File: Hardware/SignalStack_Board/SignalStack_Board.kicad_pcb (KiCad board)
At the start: 2 copper layers, 101.6 x 67.6 mm, 64 parts, among them J1 Molex_uF_SV_06, J2 RJ45_LED_Shielded, J3 Molex_uF_SV_06, Q1 SI4156DY, Q2 SI4156DY, Q3 SI4156DY, Q4 SI4156DY, Q5 SI4156DY, Q6 SI4156DY, Q7 SI4156DY, Q8 SI4156DY, U1 OKI, U2 SMAJ12CA, U3 Teensy4.1_DEV-16771, U4 TSR_1-2450, U5 IRS2005S, U6 IRS2005S, U8 IRS2005S, U9 IRS2005S

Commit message: Worked on layout a lot
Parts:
- J1: footprint MRDT_Connectors:MOLEX_uF_S_06_Vertical -> Connector_PinHeader_2.00mm:PinHeader_2x03_P2.00mm_Vertical
- moved U2 173.6 mm to (189.2, 110.0)
- moved C3 136.9 mm to (188.6, 112.8)
- moved C2 125.7 mm to (168.8, 103.6), turned to 180 degrees
- moved U5 124.7 mm to (213.9, 105.8)
- moved C4 119.5 mm to (188.6, 114.8)
- moved J1 116.2 mm to (174.8, 113.3)
- moved C6 94.9 mm to (175.8, 125.2), turned to 180 degrees
- moved U1 81.4 mm to (176.3, 101.0), turned to 180 degrees
- moved C5 80.4 mm to (188.6, 116.8)
- moved C1 78.0 mm to (173.5, 103.6), turned to 180 degrees
- moved J2 67.9 mm to (149.7, 119.2), turned to -90 degrees
- moved U4 61.1 mm to (161.0, 98.3), turned to 180 degrees
- moved Conn1 12.2 mm to (192.5, 102.9)
- moved U3 3.81 mm to (142.7, 103.9)
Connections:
- net Net-(J1-Pad1) renamed /TX+
- net Net-(J1-Pad2) renamed /TX-
- net Net-(J1-Pad5) renamed /RX-
- net Net-(J1-Pad6) renamed /RX+
- Conn1 pad 2: (no net) -> +12V
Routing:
- net +5V: track 0.00 -> 152.9 mm, vias 0 -> 2
- net GPS RX: track 0.00 -> 86.8 mm
- net GPS TX: track 0.00 -> 86.7 mm
- net +3V3: track 0.00 -> 61.9 mm, vias 0 -> 4
- net +12V: track 0.00 -> 38.2 mm
- net Net-(J1-Pad4): track 0.00 -> 28.2 mm
- net Net-(C6-Pad1): track 0.00 -> 21.8 mm, vias 0 -> 1
- net /TX-: track 0.00 -> 15.1 mm
- net /TX+: track 0.00 -> 14.3 mm
- net Net-(C6-Pad2): track 0.00 -> 13.5 mm
- net /RX+: track 0.00 -> 8.16 mm
- net /RX-: track 0.00 -> 8.05 mm
- net GND: vias 0 -> 3
- added copper zone on F.Cu, net +12V

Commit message: Worked on layout
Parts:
- Conn1: moved to B.Cu
- moved D1 138.1 mm to (163.8, 107.4)
- moved D3 118.9 mm to (157.7, 107.4)
- moved U9 118.0 mm to (207.0, 114.9)
- moved D2 99.6 mm to (177.7, 107.7)
- moved U6 98.0 mm to (207.0, 123.1)
- moved U8 83.3 mm to (207.0, 97.0)
- moved R3 79.5 mm to (157.6, 105.2)
- moved R2 77.5 mm to (181.6, 107.7)
- moved R1 67.0 mm to (167.5, 107.4), turned to 180 degrees
- moved U2 61.2 mm to (128.0, 112.0)
- moved C3 60.6 mm to (128.0, 114.8)
- moved C4 60.6 mm to (128.0, 116.8)
- moved C5 60.6 mm to (128.0, 118.9)
- moved Conn1 8.00 mm to (184.5, 102.9)
- moved U5 7.04 mm to (206.9, 104.9)
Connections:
- U3 pad 18: IMU Data -> I2C SDA
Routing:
- net I2C SDA: track 0.00 -> 77.4 mm, vias 0 -> 2
- net I2C SCL: track 0.00 -> 74.4 mm, vias 0 -> 1
- net Coil1+: track 0.00 -> 49.7 mm, vias 0 -> 2
- net Coil1-: track 0.00 -> 47.8 mm, vias 0 -> 3
- net Coil2-: track 0.00 -> 45.1 mm, vias 0 -> 2
- net Coil2+: track 0.00 -> 44.3 mm, vias 0 -> 3
- net +5V: track 152.9 -> 128.0 mm, vias 2 -> 4
- net +12V: track 38.2 -> 21.8 mm
- net Net-(D3-Pad2): track 0.00 -> 2.31 mm
- net +3V3: track 61.9 -> 64.2 mm
- net Net-(D2-Pad2): track 0.00 -> 2.14 mm
- net Net-(D1-Pad2): track 0.00 -> 1.92 mm
- net GND: track 0.00 -> 0.20 mm, vias 3 -> 4

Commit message: Finished layout
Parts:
- added G***: LOGO, MRDT_Silkscreens:0_MRDT_Logo_20mm, B.Cu at (183.4, 118.5)
- moved R16 195.2 mm to (228.2, 131.2), turned to 180 degrees
- moved D4 183.8 mm to (205.0, 100.8), turned to 180 degrees
- moved D8 183.5 mm to (204.3, 92.1), turned to 90 degrees
- moved D5 179.5 mm to (205.0, 118.7), turned to 180 degrees
- moved R5 179.3 mm to (209.0, 118.7), turned to 180 degrees
- moved D11 175.0 mm to (205.0, 111.0), turned to 180 degrees
- moved R7 171.3 mm to (209.0, 126.9), turned to 180 degrees
- moved D6 170.5 mm to (205.0, 108.7), turned to 180 degrees
- moved R15 168.3 mm to (223.5, 89.0)
- moved D9 167.4 mm to (218.1, 127.1)
- moved R9 167.0 mm to (214.5, 108.7)
- moved D10 164.1 mm to (206.8, 92.1), turned to 90 degrees
- moved C11 161.3 mm to (230.4, 119.4), turned to 90 degrees
- moved D7 158.7 mm to (205.0, 126.9), turned to 180 degrees
- moved C8 154.7 mm to (218.1, 128.9)
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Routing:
- net +12V: track 21.8 -> 163.7 mm
- net /M+: track 0.00 -> 114.2 mm, vias 0 -> 5
- net /M-: track 0.00 -> 93.5 mm, vias 0 -> 5
- net Net-(R17-Pad1): track 0.00 -> 51.9 mm, vias 0 -> 2
- net Net-(Q7-Pad4): track 0.00 -> 42.4 mm, vias 0 -> 2
- net Net-(Q8-Pad4): track 0.00 -> 36.8 mm, vias 0 -> 2
- net Net-(R16-Pad1): track 0.00 -> 34.8 mm, vias 0 -> 2
- net Net-(R10-Pad1): track 0.00 -> 22.9 mm, vias 0 -> 2
- net Net-(C7-Pad1): track 0.00 -> 21.4 mm, vias 0 -> 2
- net Net-(R15-Pad1): track 0.00 -> 20.4 mm, vias 0 -> 2
- net Net-(R12-Pad1): track 0.00 -> 18.1 mm, vias 0 -> 2
- net Net-(R9-Pad1): track 0.00 -> 16.6 mm, vias 0 -> 2
- net Net-(C8-Pad1): track 0.00 -> 14.3 mm, vias 0 -> 2
- net Net-(Q5-Pad4): track 0.00 -> 11.8 mm
- net Net-(R11-Pad1): track 0.00 -> 11.4 mm, vias 0 -> 2
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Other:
- outline, holes or cut-outs redrawn
- board text added: "Coil 1"
- board text added: "Coil 2"
- board text added: "GPS"
- board text added: "Signal Stack Board, 2023 Rev 1 Mars Rover Design Team Grant Brinker"
- board text added: "Super Spicy Signal Stack Spinning System"

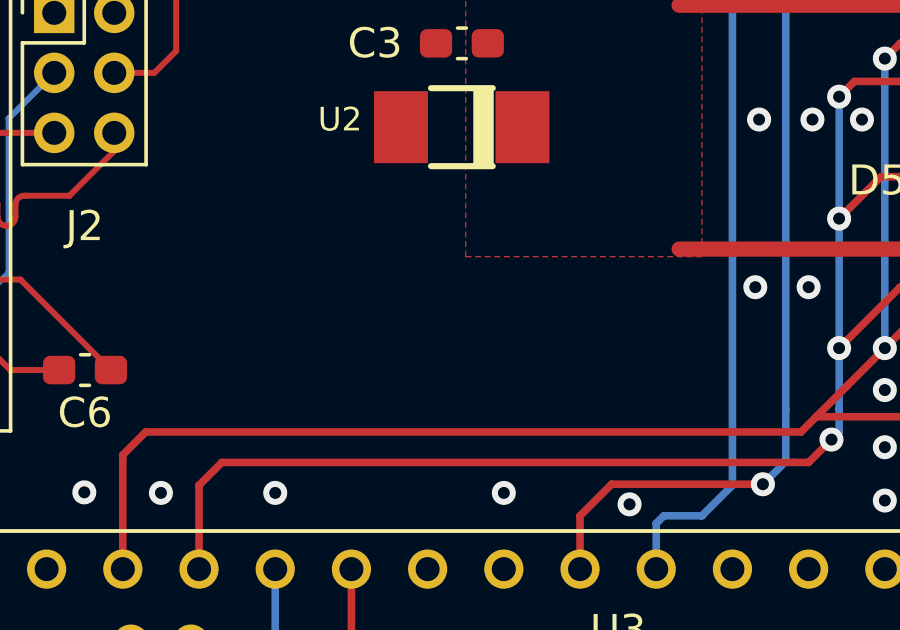
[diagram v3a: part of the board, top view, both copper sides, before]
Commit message: Added silkscreen
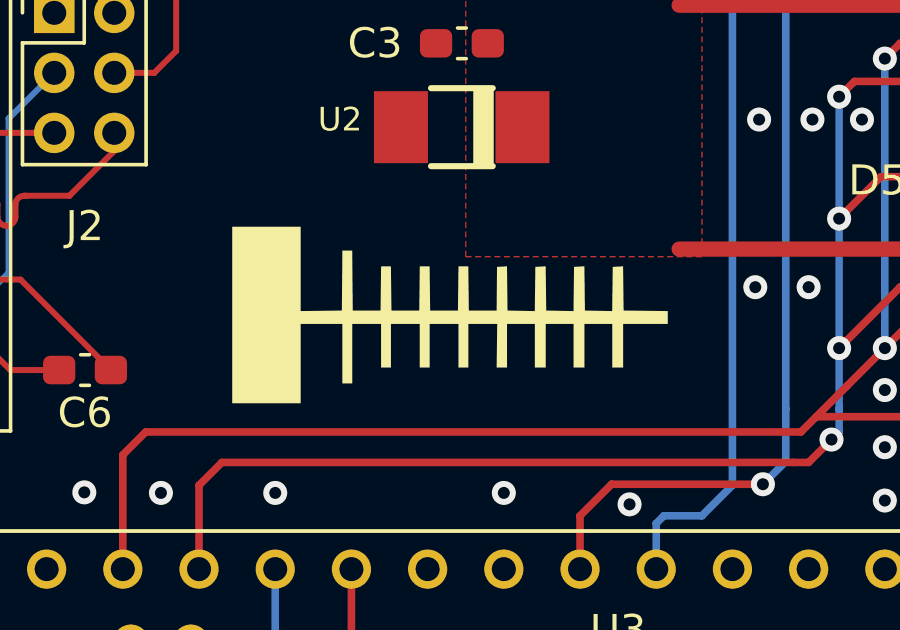
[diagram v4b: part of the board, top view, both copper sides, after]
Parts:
- added G***: LOGO, MRDT_Silkscreens:yagi, F.Cu at (188.0, 123.2)
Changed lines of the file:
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@@
     )
+  )
+  (footprint "MRDT_Silkscreens:yagi" (layer "F.Cu")
+    (at 187.96 123.19)
+    (attr board_only exclude_from_pos_files exclude_from_bom)
+    (fp_text reference "G***" (at 0 0) (layer "F.SilkS") hide
+      (effects (font (size 1.524 1.524) (thickness 0.3)))
+    )
+    (fp_text value "LOGO" (at 0.75 0) (layer "F.SilkS") hide
+      (effects (font (size 1.524 1.524) (thickness 0.3)))
+    )
+    (fp_poly (pts
+        (xy -4.994011 0.034415)
+        (xy -4.307748 0.025475)
+        (xy -3.621485 0.016536)
+        (xy -3.612732 -0.98392)
+        (xy -3.603978 -1.984375)
+        (xy -3.275189 -1.984375)
+        (xy -3.266436 -0.98392)
+        (xy -3.257683 0.016536)
+        (xy -2.331641 0.016536)
+        (xy -2.32274 -0.719336)
+        (xy -2.313839 -1.455209)
+        (xy -1.985641 -1.455209)
+        (xy -1.97674 -0.719336)
+        (xy -1.967839 0.016536)
+        (xy -1.041797 0.016536)
+        (xy -1.032896 -0.719336)
+        (xy -1.023995 -1.455209)
+        (xy -0.695797 -1.455209)
+        (xy -0.686896 -0.719336)
+        (xy -0.677995 0.016536)
+        (xy 0.248046 0.016536)
+        (xy 0.256947 -0.719336)
+        (xy 0.265848 -1.455209)
+        (xy 0.594047 -1.455209)
+        (xy 0.602948 -0.719336)
+        (xy 0.611849 0.016536)
+        (xy 1.53789 0.016536)
+        (xy 1.544146 -0.711068)
+        (xy 1.550401 -1.438672)
+        (xy 1.717141 -1.448647)
+        (xy 1.883881 -1.458621)
+        (xy 1.892787 -0.721042)
+        (xy 1.901692 0.016536)
+        (xy 2.35581 0.025734)
+        (xy 2.809927 0.034931)
+        (xy 2.818831 -0.701871)
+        (xy 2.827734 -1.438672)
+        (xy 3.000729 -1.448647)
+        (xy 3.173725 -1.458621)
+        (xy 3.182631 -0.721042)
+        (xy 3.191536 0.016536)
+        (xy 3.645653 0.025734)
+        (xy 4.099771 0.034931)
+        (xy 4.108674 -0.701871)
+        (xy 4.117578 -1.438672)
+        (xy 4.290573 -1.448647)
+        (xy 4.463569 -1.458621)
+        (xy 4.472474 -0.721042)
+        (xy 4.48138 0.016536)
+        (xy 4.935497 0.025734)
+        (xy 5.389615 0.034931)
+        (xy 5.398518 -0.701871)
+        (xy 5.407421 -1.438672)
+        (xy 5.580417 -1.448647)
+        (xy 5.753413 -1.458621)
+        (xy 5.762318 -0.721042)
+        (xy 5.771224 0.016536)
+        (xy 7.242968 0.034338)
+        (xy 7.242968 0.463021)
+        (xy 5.754687 0.463021)
+        (xy 5.754687 1.918229)
+        (xy 5.390885 1.918229)
+        (xy 5.390885 0.463021)
+        (xy 4.464843 0.463021)
+        (xy 4.464843 1.918229)
+        (xy 4.101041 1.918229)
+        (xy 4.101041 0.463021)
+        (xy 3.175 0.463021)
+        (xy 3.175 1.918229)
+        (xy 2.811198 1.918229)
+        (xy 2.811198 0.463021)
+        (xy 1.885156 0.463021)
+        (xy 1.885156 1.918229)
+        (xy 1.53789 1.918289)
+        (xy 1.556886 0.463021)
+        (xy 0.595312 0.463021)
+        (xy 0.595312 1.918229)
+        (xy 0.264583 1.918229)
+        (xy 0.264583 0.463021)
+        (xy -0.694532 0.463021)
+        (xy -0.694532 1.918229)
+        (xy -1.025261 1.918229)
+        (xy -1.025261 0.463021)
+        (xy -1.984375 0.463021)
+        (xy -1.984375 1.918229)
+        (xy -2.315105 1.918229)
+        (xy -2.315105 0.463021)
+        (xy -3.274219 0.463021)
+        (xy -3.274219 2.447396)
+        (xy -3.604948 2.447396)
+        (xy -3.604948 0.463021)
+        (xy -4.994011 0.463021)
+        (xy -4.994011 3.108854)
+        (xy -7.276042 3.108854)
+        (xy -7.276042 -2.778125)
+        (xy -4.994011 -2.778125)
+      ) (layer "F.SilkS") (width 0) (fill solid))
   )
   (footprint "MRDT_Shields:Teensy_4_1_Vertical" (layer "F.Cu")

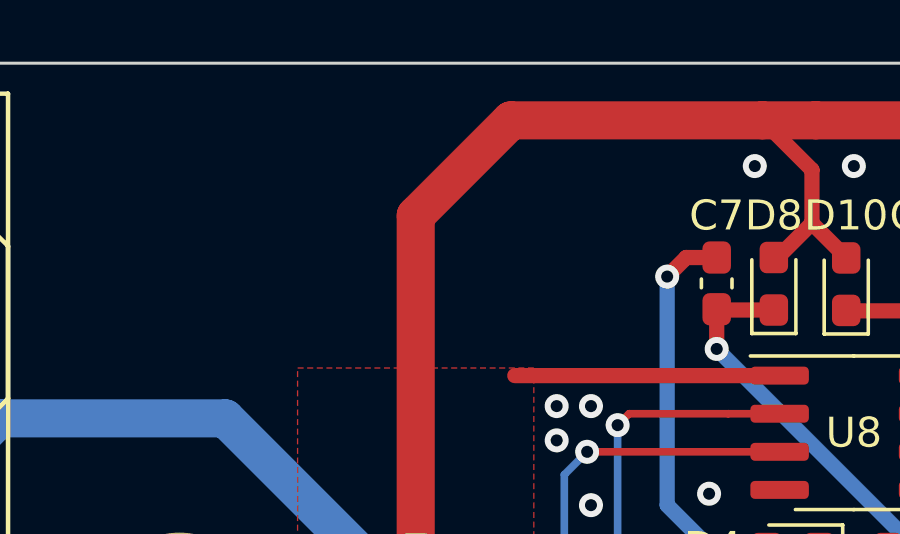
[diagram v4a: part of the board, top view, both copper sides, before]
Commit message: Added more via stitching
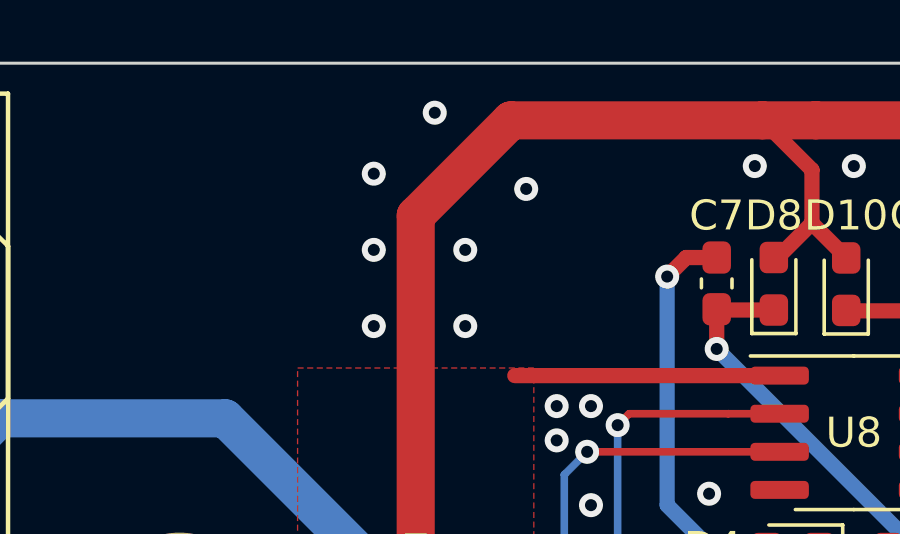
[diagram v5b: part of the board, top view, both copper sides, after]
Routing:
- net GND: vias 74 -> 81
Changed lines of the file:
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@@
   (via (at 198.247 110.109) (size 0.8) (drill 0.4) (layers "F.Cu" "B.Cu") (free) (net 2))
   (via (at 202.438 125.857) (size 0.8) (drill 0.4) (layers "F.Cu" "B.Cu") (free) (net 2))
+  (via (at 193.04 86.36) (size 0.8) (drill 0.4) (layers "F.Cu" "B.Cu") (free) (net 2))
   (via (at 214.757 127.762) (size 0.8) (drill 0.4) (layers "F.Cu" "B.Cu") (free) (net 2))
   (via (at 198.247 116.84) (size 0.8) (drill 0.4) (layers "F.Cu" "B.Cu") (free) (net 2))
@@
   (via (at 212.217 104.394) (size 0.8) (drill 0.4) (layers "F.Cu" "B.Cu") (free) (net 2))
   (via (at 203.708 88.138) (size 0.8) (drill 0.4) (layers "F.Cu" "B.Cu") (free) (net 2))
+  (via (at 196.088 88.9) (size 0.8) (drill 0.4) (layers "F.Cu" "B.Cu") (free) (net 2))
   (via (at 207.518 141.986) (size 0.8) (drill 0.4) (layers "F.Cu" "B.Cu") (free) (net 2))
   (via (at 199.898 141.986) (size 0.8) (drill 0.4) (layers "F.Cu" "B.Cu") (free) (net 2))
+  (via (at 194.056 93.472) (size 0.8) (drill 0.4) (layers "F.Cu" "B.Cu") (free) (net 2))
   (via (at 177.292 111.252) (size 0.8) (drill 0.4) (layers "F.Cu" "B.Cu") (free) (net 2))
+  (via (at 191.008 88.392) (size 0.8) (drill 0.4) (layers "F.Cu" "B.Cu") (free) (net 2))
   (via (at 220.853 109.728) (size 0.8) (drill 0.4) (layers "F.Cu" "B.Cu") (free) (net 2))
+  (via (at 191.008 90.932) (size 0.8) (drill 0.4) (layers "F.Cu" "B.Cu") (free) (net 2))
   (via (at 235.458 144.526) (size 0.8) (drill 0.4) (layers "F.Cu" "B.Cu") (free) (net 2))
   (via (at 207.250415 129.523008) (size 0.8) (drill 0.4) (layers "F.Cu" "B.Cu") (free) (net 2))
@@
   (via (at 223.266 93.345) (size 0.8) (drill 0.4) (layers "F.Cu" "B.Cu") (free) (net 2))
   (via (at 197.104 97.282) (size 0.8) (drill 0.4) (layers "F.Cu" "B.Cu") (free) (net 2))
+  (via (at 191.008 93.472) (size 0.8) (drill 0.4) (layers "F.Cu" "B.Cu") (free) (net 2))
   (via (at 207.518 144.526) (size 0.8) (drill 0.4) (layers "F.Cu" "B.Cu") (free) (net 2))
   (via (at 212.09 134.366) (size 0.8) (drill 0.4) (layers "F.Cu" "B.Cu") (free) (net 2))
@@
   (via (at 204.978 129.54) (size 0.8) (drill 0.4) (layers "F.Cu" "B.Cu") (free) (net 2))
   (via (at 198.247 105.029) (size 0.8) (drill 0.4) (layers "F.Cu" "B.Cu") (free) (net 2))
+  (via (at 194.056 90.932) (size 0.8) (drill 0.4) (layers "F.Cu" "B.Cu") (free) (net 2))
   (via (at 211.963 96.393) (size 0.8) (drill 0.4) (layers "F.Cu" "B.Cu") (free) (net 2))
   (via (at 207.264 134.366) (size 0.8) (drill 0.4) (layers "F.Cu" "B.Cu") (free) (net 2))
